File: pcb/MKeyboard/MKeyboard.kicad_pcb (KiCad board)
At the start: 6 copper layers, 57.1 x 88.8 mm, 90 parts, among them J1 USB_C_Receptacle_USB2.0, SW0 SW_Push, SW1 SW_Push, SW10 SW_Push, SW11 SW_Push, SW12 SW_Push, SW2 SW_Push, SW20 SW_Push, SW21 SW_Push, SW22 SW_Push, SW3 SW_DIP_x01, SW30 SW_Push, SW31 SW_Push, SW32 SW_Push, SW40 SW_Push, SW41 SW_Push, SW42 SW_Push, U1 AT90USB646-AU, Y1 Crystal_GND24

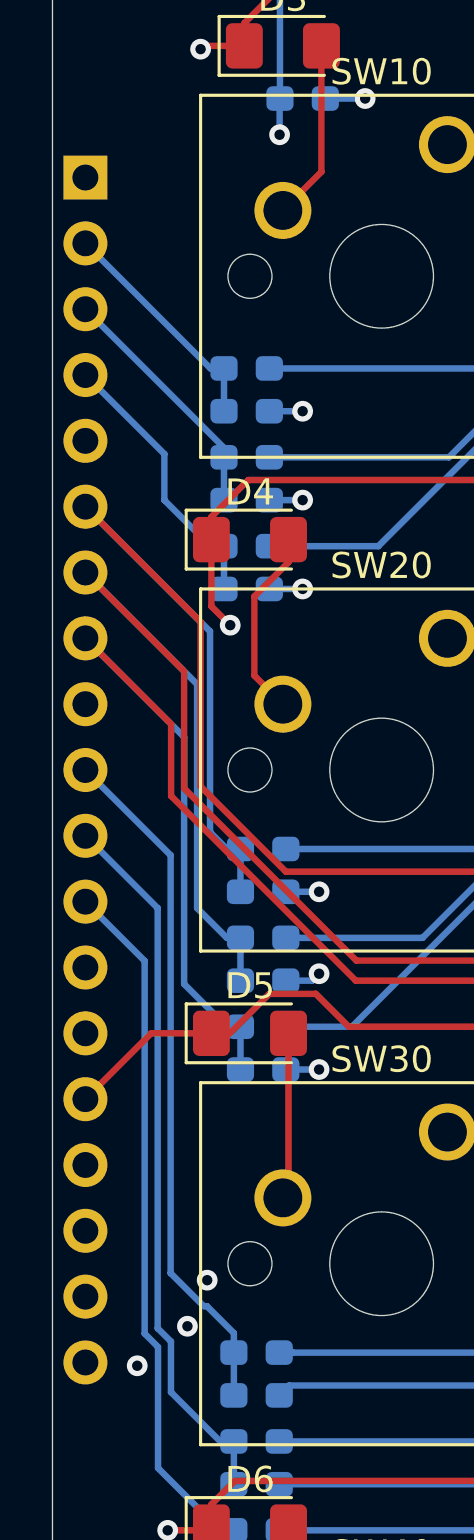
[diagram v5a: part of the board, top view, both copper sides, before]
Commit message: fixed orientation of left connector
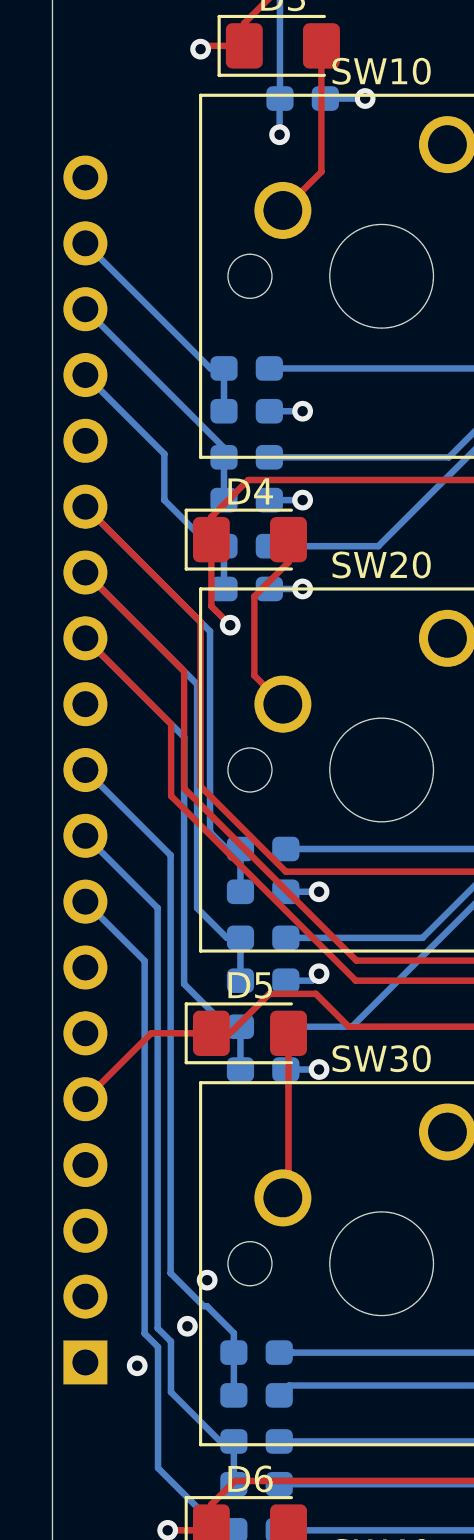
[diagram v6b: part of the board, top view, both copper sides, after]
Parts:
- moved JL1 45.7 mm to (77.5, 146.1), turned to 0 degrees
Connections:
- JL1 pad 11: /con_l0_1 -> GND
- JL1 pad 12: /con_l0_0 -> /con_l1_0
- JL1 pad 13: GND -> /con_l1_1
- JL1 pad 14: /row4 -> /con_l1_2
- JL1 pad 15: /row3 -> GND
- JL1 pad 16: /row2 -> /con_l2_0
- JL1 pad 17: /row1 -> /con_l2_1
- JL1 pad 18: /row0 -> /con_l2_2
- JL1 pad 2: /con_l2_2 -> /row0
- JL1 pad 3: /con_l2_1 -> /row1
- JL1 pad 4: /con_l2_0 -> /row2
- JL1 pad 5: GND -> /row3
- JL1 pad 6: /con_l1_2 -> /row4
- JL1 pad 7: /con_l1_1 -> GND
- JL1 pad 8: /con_l1_0 -> /con_l0_0
- JL1 pad 9: GND -> /con_l0_1
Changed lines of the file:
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@@
   )
   (module Connector_PinSocket_2.54mm:PinSocket_1x19_P2.54mm_Horizontal (layer B.Cu)
-    (at 77.47 100.33 180)
+    (at 77.47 146.05)
     (descr "Through hole angled socket strip, 1x19, 2.54mm pitch, 8.51mm socket length, single row (from Kicad 4.0.7), script generated")
     (tags "Through hole angled socket strip THT 1x19 2.54mm single row")
@@
       (effects (font (size 1 1) (thickness 0.15)) (justify mirror))
     )
-    (pad 1 thru_hole rect (at 0 0 180) (size 1.7 1.7) (drill 1) (layers *.Cu *.Mask)
+    (pad 1 thru_hole rect (at 0 0) (size 1.7 1.7) (drill 1) (layers *.Cu *.Mask)
       (net 1 GND))
-    (pad 2 thru_hole oval (at 0 -2.54 180) (size 1.7 1.7) (drill 1) (layers *.Cu *.Mask)
+    (pad 2 thru_hole oval (at 0 -2.54) (size 1.7 1.7) (drill 1) (layers *.Cu *.Mask)
+      (net 7 /row0))
+    (pad 3 thru_hole oval (at 0 -5.08) (size 1.7 1.7) (drill 1) (layers *.Cu *.Mask)
+      (net 10 /row1))
+    (pad 4 thru_hole oval (at 0 -7.62) (size 1.7 1.7) (drill 1) (layers *.Cu *.Mask)
+      (net 11 /row2))
+    (pad 5 thru_hole oval (at 0 -10.16) (size 1.7 1.7) (drill 1) (layers *.Cu *.Mask)
+      (net 14 /row3))
+    (pad 6 thru_hole oval (at 0 -12.7) (size 1.7 1.7) (drill 1) (layers *.Cu *.Mask)
+      (net 16 /row4))
+    (pad 7 thru_hole oval (at 0 -15.24) (size 1.7 1.7) (drill 1) (layers *.Cu *.Mask)
+      (net 1 GND))
+    (pad 8 thru_hole oval (at 0 -17.78) (size 1.7 1.7) (drill 1) (layers *.Cu *.Mask)
+      (net 37 /con_l0_0))
+    (pad 9 thru_hole oval (at 0 -20.32) (size 1.7 1.7) (drill 1) (layers *.Cu *.Mask)
+      (net 36 /con_l0_1))
+    (pad 10 thru_hole oval (at 0 -22.86) (size 1.7 1.7) (drill 1) (layers *.Cu *.Mask)
+      (net 35 /con_l0_2))
+    (pad 11 thru_hole oval (at 0 -25.4) (size 1.7 1.7) (drill 1) (layers *.Cu *.Mask)
+      (net 1 GND))
+    (pad 12 thru_hole oval (at 0 -27.94) (size 1.7 1.7) (drill 1) (layers *.Cu *.Mask)
+      (net 34 /con_l1_0))
+    (pad 13 thru_hole oval (at 0 -30.48) (size 1.7 1.7) (drill 1) (layers *.Cu *.Mask)
+      (net 33 /con_l1_1))
+    (pad 14 thru_hole oval (at 0 -33.02) (size 1.7 1.7) (drill 1) (layers *.Cu *.Mask)
+      (net 32 /con_l1_2))
+    (pad 15 thru_hole oval (at 0 -35.56) (size 1.7 1.7) (drill 1) (layers *.Cu *.Mask)
+      (net 1 GND))
+    (pad 16 thru_hole oval (at 0 -38.1) (size 1.7 1.7) (drill 1) (layers *.Cu *.Mask)
+      (net 31 /con_l2_0))
+    (pad 17 thru_hole oval (at 0 -40.64) (size 1.7 1.7) (drill 1) (layers *.Cu *.Mask)
+      (net 30 /con_l2_1))
+    (pad 18 thru_hole oval (at 0 -43.18) (size 1.7 1.7) (drill 1) (layers *.Cu *.Mask)
       (net 29 /con_l2_2))
-    (pad 3 thru_hole oval (at 0 -5.08 180) (size 1.7 1.7) (drill 1) (layers *.Cu *.Mask)
-      (net 30 /con_l2_1))
-    (pad 4 thru_hole oval (at 0 -7.62 180) (size 1.7 1.7) (drill 1) (layers *.Cu *.Mask)
-      (net 31 /con_l2_0))
-    (pad 5 thru_hole oval (at 0 -10.16 180) (size 1.7 1.7) (drill 1) (layers *.Cu *.Mask)
-      (net 1 GND))
-    (pad 6 thru_hole oval (at 0 -12.7 180) (size 1.7 1.7) (drill 1) (layers *.Cu *.Mask)
-      (net 32 /con_l1_2))
-    (pad 7 thru_hole oval (at 0 -15.24 180) (size 1.7 1.7) (drill 1) (layers *.Cu *.Mask)
-      (net 33 /con_l1_1))
-    (pad 8 thru_hole oval (at 0 -17.78 180) (size 1.7 1.7) (drill 1) (layers *.Cu *.Mask)
-      (net 34 /con_l1_0))
-    (pad 9 thru_hole oval (at 0 -20.32 180) (size 1.7 1.7) (drill 1) (layers *.Cu *.Mask)
-      (net 1 GND))
-    (pad 10 thru_hole oval (at 0 -22.86 180) (size 1.7 1.7) (drill 1) (layers *.Cu *.Mask)
-      (net 35 /con_l0_2))
-    (pad 11 thru_hole oval (at 0 -25.4 180) (size 1.7 1.7) (drill 1) (layers *.Cu *.Mask)
-      (net 36 /con_l0_1))
-    (pad 12 thru_hole oval (at 0 -27.94 180) (size 1.7 1.7) (drill 1) (layers *.Cu *.Mask)
-      (net 37 /con_l0_0))
-    (pad 13 thru_hole oval (at 0 -30.48 180) (size 1.7 1.7) (drill 1) (layers *.Cu *.Mask)
-      (net 1 GND))
-    (pad 14 thru_hole oval (at 0 -33.02 180) (size 1.7 1.7) (drill 1) (layers *.Cu *.Mask)
-      (net 16 /row4))
-    (pad 15 thru_hole oval (at 0 -35.56 180) (size 1.7 1.7) (drill 1) (layers *.Cu *.Mask)
-      (net 14 /row3))
-    (pad 16 thru_hole oval (at 0 -38.1 180) (size 1.7 1.7) (drill 1) (layers *.Cu *.Mask)
-      (net 11 /row2))
-    (pad 17 thru_hole oval (at 0 -40.64 180) (size 1.7 1.7) (drill 1) (layers *.Cu *.Mask)
-      (net 10 /row1))
-    (pad 18 thru_hole oval (at 0 -43.18 180) (size 1.7 1.7) (drill 1) (layers *.Cu *.Mask)
-      (net 7 /row0))
-    (pad 19 thru_hole oval (at 0 -45.72 180) (size 1.7 1.7) (drill 1) (layers *.Cu *.Mask)
+    (pad 19 thru_hole oval (at 0 -45.72) (size 1.7 1.7) (drill 1) (layers *.Cu *.Mask)
       (net 1 GND))
     (model ${KISYS3DMOD}/Connector_PinSocket_2.54mm.3dshapes/PinSocket_1x19_P2.54mm_Horizontal.wrl
@@
   (gr_line (start 76.2 75.057) (end 133.35 75.057) (layer Edge.Cuts) (width 0.05))
   (via (at 126.365 97.536) (size 0.8) (drill 0.4) (layers F.Cu B.Cu) (net 1))
-  (via (at 88.265 97.282) (size 0.8) (drill 0.4) (layers F.Cu B.Cu) (net 2))
-  (via (at 100.203 78.486) (size 0.8) (drill 0.4) (layers F.Cu B.Cu) (net 2))
-  (via (at 96.012 78.486) (size 0.8) (drill 0.4) (layers F.Cu B.Cu) (net 2))
-  (via (at 95.885 82.677) (size 0.8) (drill 0.4) (layers F.Cu B.Cu) (net 2))
   (via (at 98.171 91.694) (size 0.8) (drill 0.4) (layers F.Cu B.Cu) (net 1))
   (via (at 118.11 82.677) (size 0.8) (drill 0.4) (layers F.Cu B.Cu) (net 1))
   (via (at 115.189 82.55) (size 0.8) (drill 0.4) (layers F.Cu B.Cu) (net 1))
-  (via (at 116.205 90.932) (size 0.8) (drill 0.4) (layers F.Cu B.Cu) (net 2))
   (via (at 105.537 90.805) (size 0.8) (drill 0.4) (layers F.Cu B.Cu) (net 1))
-  (via (at 107.696 90.805) (size 0.8) (drill 0.4) (layers F.Cu B.Cu) (net 2))
   (via (at 109.855 90.805) (size 0.8) (drill 0.4) (layers F.Cu B.Cu) (net 1))
   (segment (start 102.053 79.803) (end 102.423 80.173) (width 0.25) (layer In3.Cu) (net 1))
@@
   (segment (start 110.476 90.184) (end 109.855 90.805) (width 0.25) (layer B.Cu) (net 1))
   (segment (start 110.476 89.408) (end 110.476 90.184) (width 0.25) (layer B.Cu) (net 1))
-  (segment (start 100.223 81.153) (end 100.223 79.803) (width 0.25) (layer In3.Cu) (net 2))
-  (segment (start 95.973 81.153) (end 95.973 79.803) (width 0.25) (layer In3.Cu) (net 2))
-  (segment (start 108.726 89.775) (end 107.696 90.805) (width 0.25) (layer B.Cu) (net 2))
-  (segment (start 108.726 89.408) (end 108.726 89.775) (width 0.25) (layer B.Cu) (net 2))
-  (segment (start 107.423 91.078) (end 107.423 92.503) (width 0.25) (layer B.Cu) (net 2))
-  (segment (start 107.696 90.805) (end 107.423 91.078) (width 0.25) (layer B.Cu) (net 2))
-  (segment (start 117.743 90.932) (end 116.205 90.932) (width 0.25) (layer B.Cu) (net 2))
   (via (at 127.635 95.631) (size 0.8) (drill 0.4) (layers F.Cu B.Cu) (net 1))
   (segment (start 125.646 95.631) (end 125.502 95.487) (width 0.25) (layer B.Cu) (net 1))
@@
   (segment (start 117.57 98.203) (end 117.954 98.203) (width 0.25) (layer B.Cu) (net 1))
   (via (at 117.57 98.203) (size 0.8) (drill 0.4) (layers F.Cu B.Cu) (net 1))
+  (via (at 88.265 97.282) (size 0.8) (drill 0.4) (layers F.Cu B.Cu) (net 2))
+  (via (at 100.203 78.486) (size 0.8) (drill 0.4) (layers F.Cu B.Cu) (net 2))
+  (via (at 96.012 78.486) (size 0.8) (drill 0.4) (layers F.Cu B.Cu) (net 2))
+  (via (at 95.885 82.677) (size 0.8) (drill 0.4) (layers F.Cu B.Cu) (net 2))
+  (via (at 116.205 90.932) (size 0.8) (drill 0.4) (layers F.Cu B.Cu) (net 2))
+  (via (at 107.696 90.805) (size 0.8) (drill 0.4) (layers F.Cu B.Cu) (net 2))
+  (segment (start 100.223 81.153) (end 100.223 79.803) (width 0.25) (layer In3.Cu) (net 2))
+  (segment (start 95.973 81.153) (end 95.973 79.803) (width 0.25) (layer In3.Cu) (net 2))
+  (segment (start 108.726 89.775) (end 107.696 90.805) (width 0.25) (layer B.Cu) (net 2))
+  (segment (start 108.726 89.408) (end 108.726 89.775) (width 0.25) (layer B.Cu) (net 2))
+  (segment (start 107.423 91.078) (end 107.423 92.503) (width 0.25) (layer B.Cu) (net 2))
+  (segment (start 107.696 90.805) (end 107.423 91.078) (width 0.25) (layer B.Cu) (net 2))
+  (segment (start 117.743 90.932) (end 116.205 90.932) (width 0.25) (layer B.Cu) (net 2))
   (segment (start 100.587 90.297) (end 100.062 90.297) (width 0.25) (layer B.Cu) (net 2))
   (segment (start 102.217 90.297) (end 101.6 90.297) (width 0.25) (layer B.Cu) (net 2))
